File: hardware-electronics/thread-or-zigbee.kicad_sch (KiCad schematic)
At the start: 25 parts, among them U5 CP2102N-A02-GQFN20, U7 EFR32MG21B020F1024IM32-B

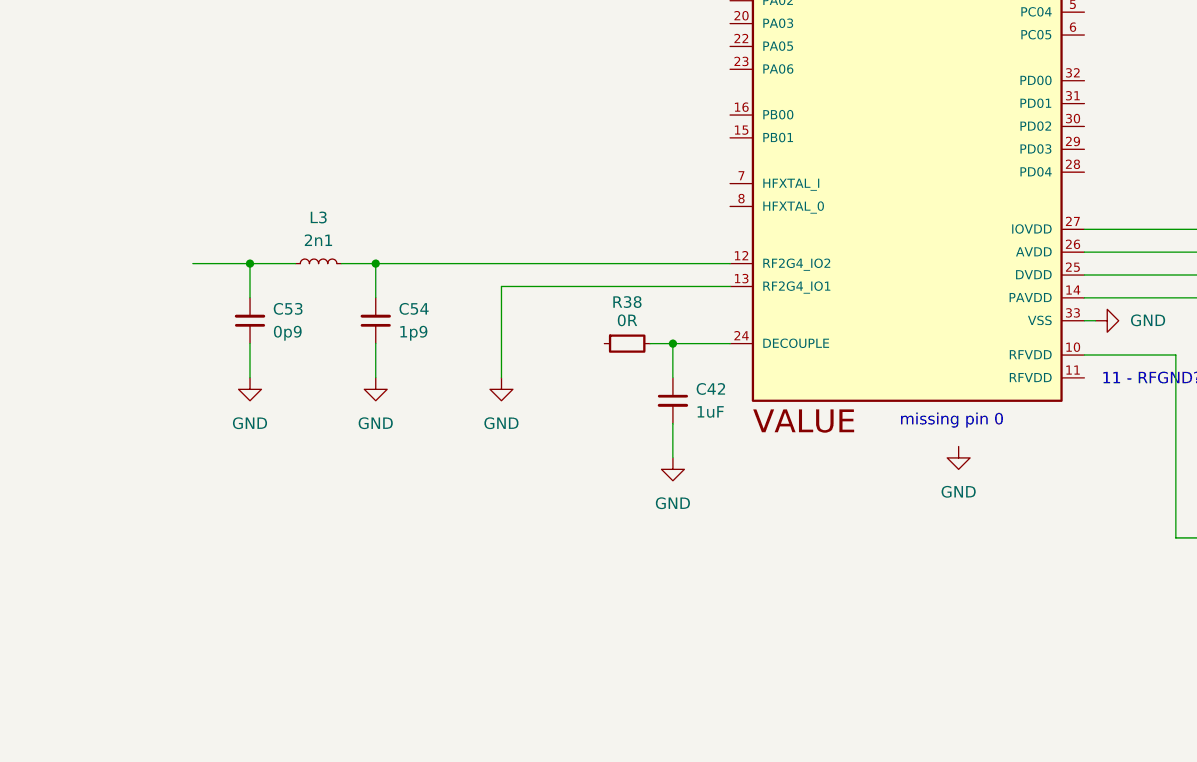
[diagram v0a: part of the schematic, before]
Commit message: #12 WIP SCH thread/zigbee working on EFR32MG21 add crystal oscillator
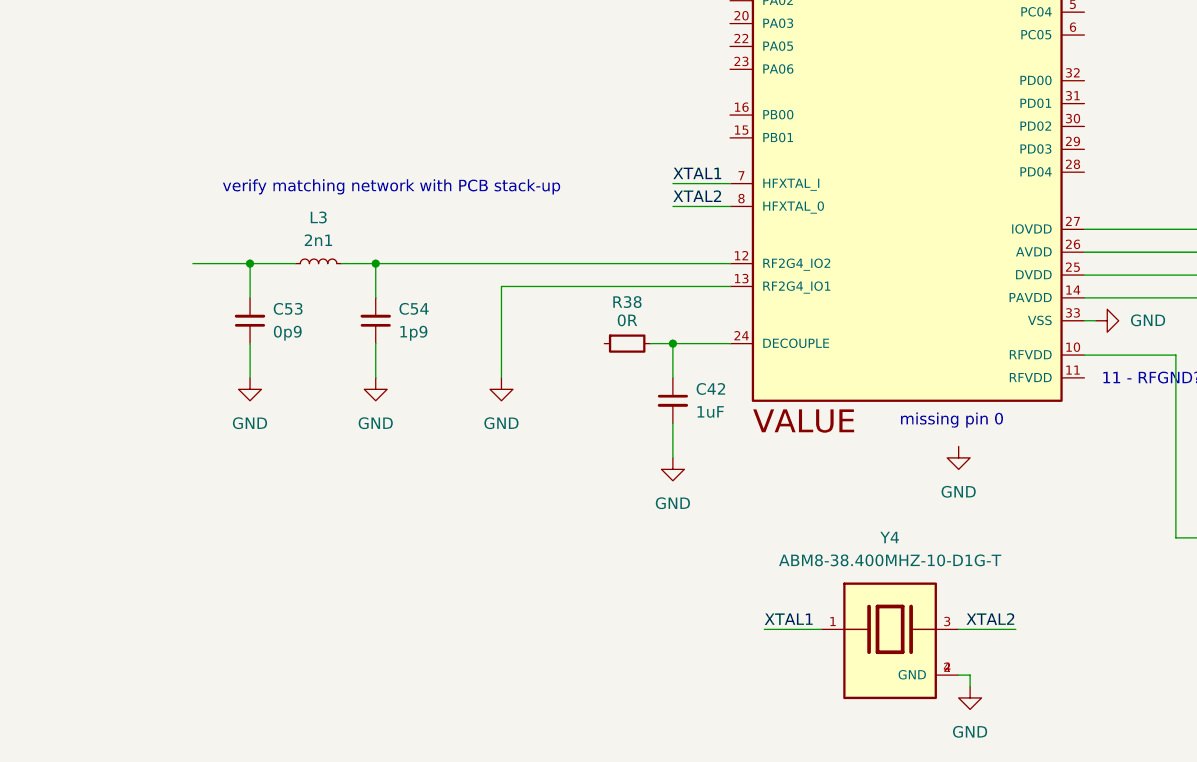
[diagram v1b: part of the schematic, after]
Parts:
- added Y4: ABM8-38.400MHZ-10-D1G-T, ABM8-38.400MHZ-10-D1G-T:XTAL_ABM8-38.400MHZ-10-D1G-T, symbol M2SmartHomeSymbols:ABM8-38.400MHZ-10-D1G-T
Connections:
- net GND: now also Y4.2 (GND), Y4.4 (GND)
- net XTAL1: now reaches U7.7 (HFXTAL_I)
- net XTAL1: now also Y4.1
- net XTAL2: now reaches U7.8 (HFXTAL_0)
- net XTAL2: now also Y4.3
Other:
- note added: "verify matching network with PCB stack-up"

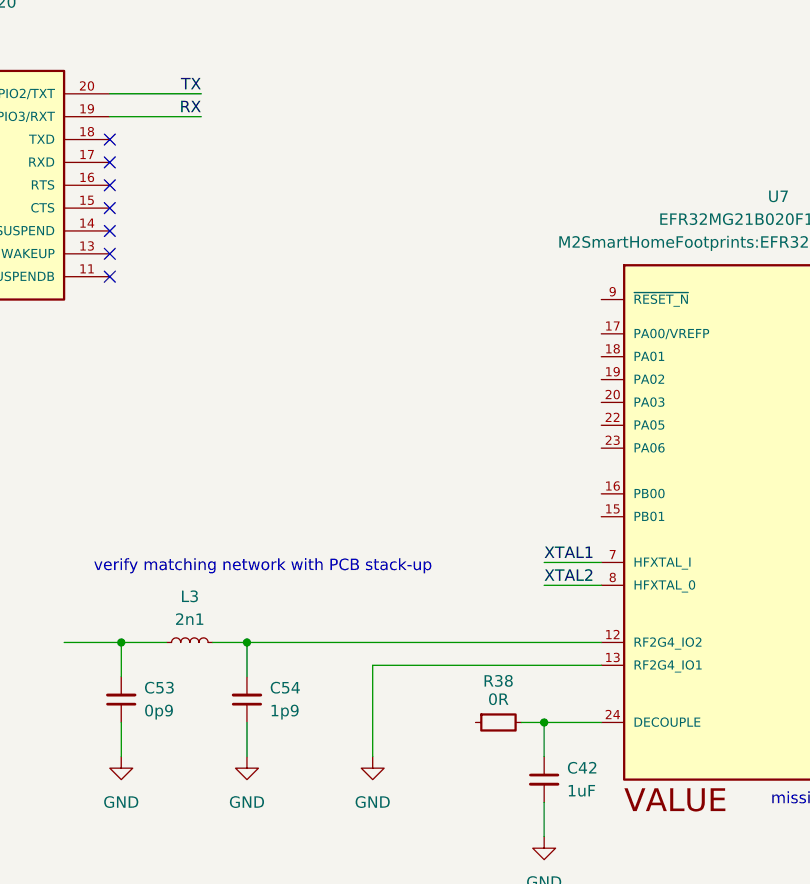
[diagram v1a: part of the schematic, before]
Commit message: #12 WIP SCH thread/zigbee working on EFR32MG21 connected decouple
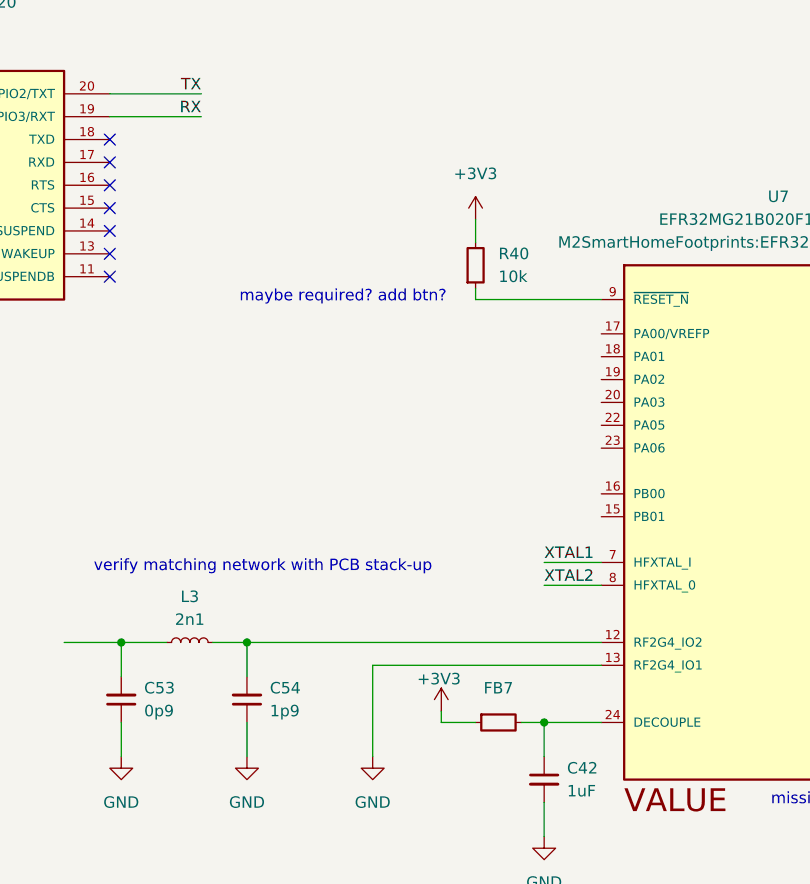
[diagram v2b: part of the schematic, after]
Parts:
- removed R38: R_0_0402, R_0_0402:R_0402_1005Metric, symbol M2SmartHomeSymbols:R_0_0402
- added FB7: FB_120R_0603, FB_120R_0603:FB_0603_1608Metric, symbol M2SmartHomeSymbols:FB_120R_0603
- added R40: R_10k_0402, R_10k_0402:R_0402_1005Metric, symbol M2SmartHomeSymbols:R_10k_0402
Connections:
- net +3V3: now also FB7.1, R40.2
- net at C42.1, U7.24 (DECOUPLE): now also FB7.2
- net at U7.9 (~{RESET_N}): now also R40.1
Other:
- note added: "maybe required? add btn?"

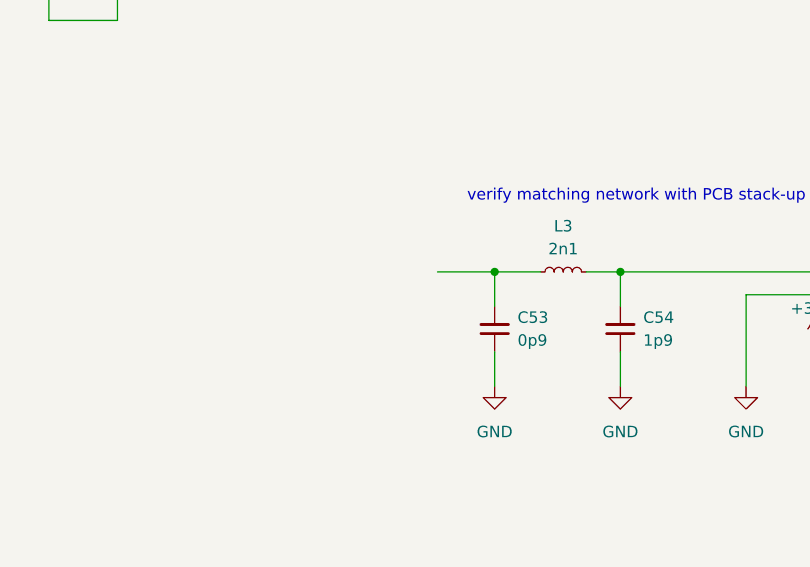
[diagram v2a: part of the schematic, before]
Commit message: #12 WIP SCH thread/zigbee working on EFR32MG21 add U.FL connector
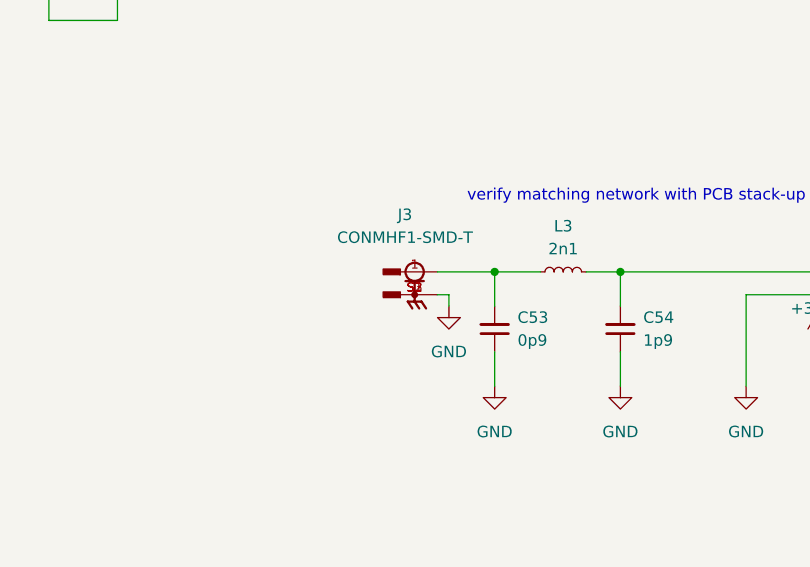
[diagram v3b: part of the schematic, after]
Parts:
- added J3: CONMHF1-SMD-T, CONMHF1-SMD-T:LINX_CONMHF1-SMD-T, symbol M2SmartHomeSymbols:CONMHF1-SMD-T
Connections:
- net GND: now also J3.S1, J3.S2, J3.S3
- net at C53.2, L3.1: now also J3.1

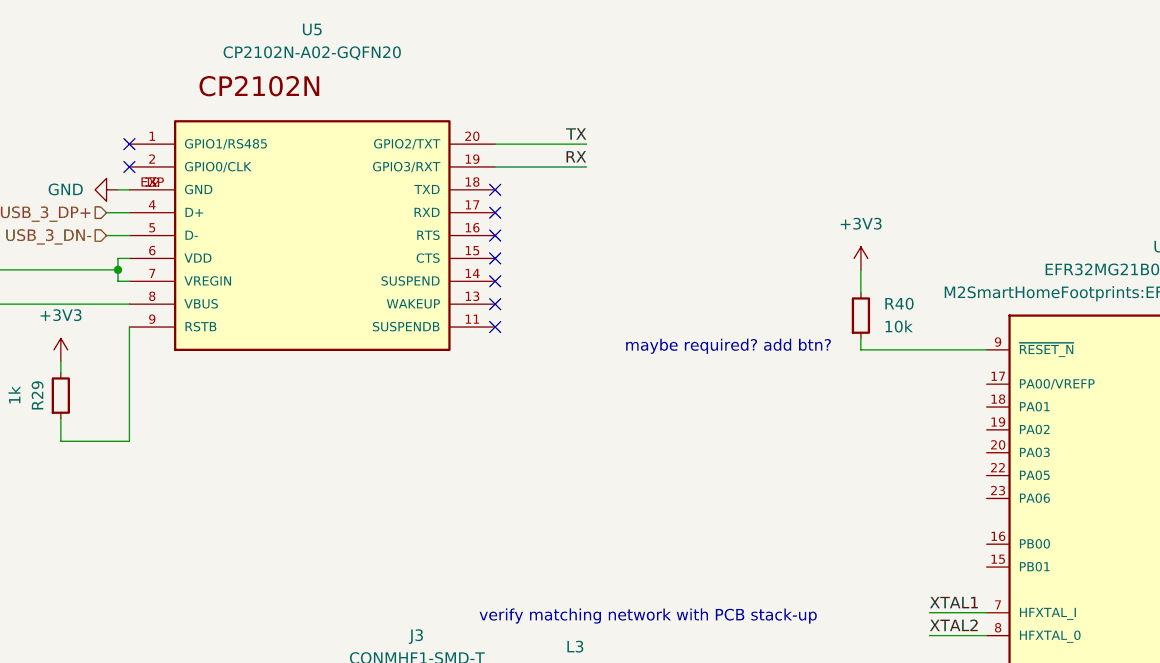
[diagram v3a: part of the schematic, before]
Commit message: [#12] SCH thread/zigbee correct UART
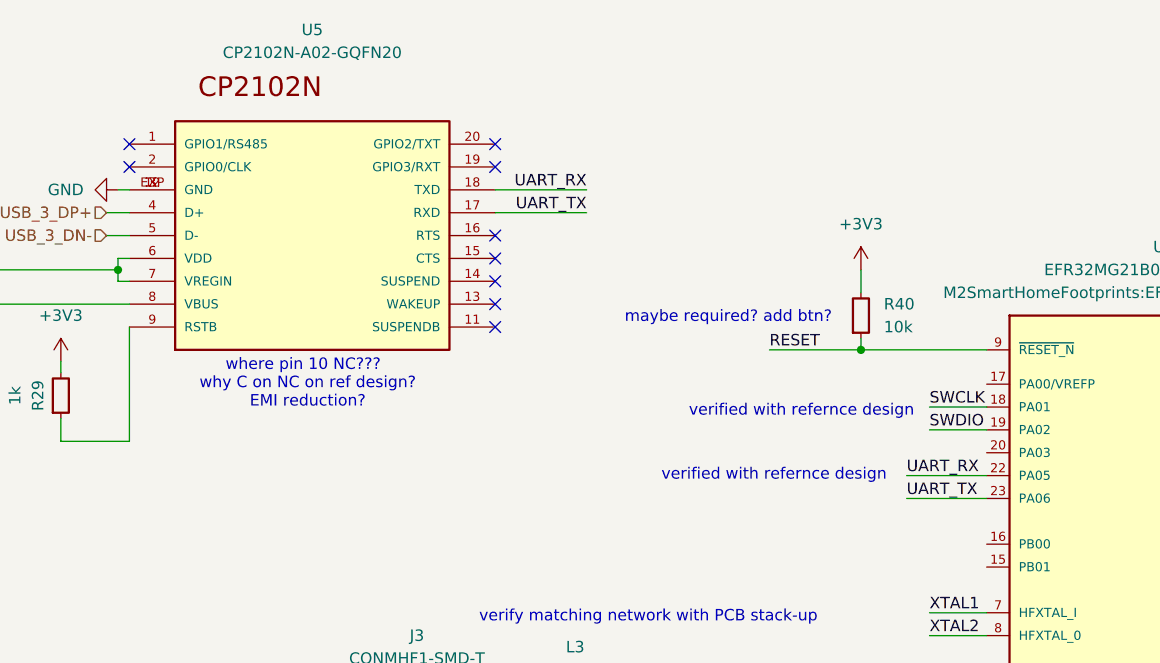
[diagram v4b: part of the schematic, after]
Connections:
- net SWCLK: now reaches U7.18 (PA01)
- net SWDIO: now reaches U7.19 (PA02)
- net UART_RX: now reaches U7.22 (PA05)
- net UART_RX: now also U5.18 (TXD)
- net UART_TX: now reaches U7.23 (PA06)
- net UART_TX: now also U5.17 (RXD)
- net RESET: now reaches R40.1, U7.9 (~{RESET_N})
- net RX: no longer names the net of U5.19 (GPIO3/RXT)
- net TX: no longer names the net of U5.20 (GPIO2/TXT)
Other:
- note added: "verified with refernce design"
- note added: "where pin 10 NC???"
- note added: "why C on NC on ref design? EMI reduction?"
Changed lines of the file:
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@@
+	)
+	(junction
+		(at 148.59 58.42)
+		(diameter 0)
+		(color 0 0 0 0)
 	)
 	(junction
@@
 	)
 	(no_connect
+		(at 107.95 38.1)
+	)
+	(no_connect
 		(at 107.95 50.8)
 	)
@@
 	)
 	(no_connect
-		(at 107.95 40.64)
-	)
-	(no_connect
-		(at 107.95 43.18)
+		(at 107.95 35.56)
 	)
 	(wire
@@
 	(wire
 		(pts
+			(xy 156.21 67.31) (xy 162.56 67.31)
+		)
+		(stroke
+			(width 0)
+			(type default)
+		)
+	)
+	(wire
+		(pts
 			(xy 166.37 137.16) (xy 172.72 137.16)
 		)
@@
 	(wire
 		(pts
+			(xy 156.21 64.77) (xy 162.56 64.77)
+		)
+		(stroke
+			(width 0)
+			(type default)
+		)
+	)
+	(wire
+		(pts
 			(xy 267.97 104.14) (xy 267.97 106.68)
 		)
@@
 	(wire
 		(pts
-			(xy 107.95 35.56) (xy 118.11 35.56)
-		)
-		(stroke
-			(width 0)
-			(type default)
-		)
-	)
-	(wire
-		(pts
 			(xy 153.67 105.41) (xy 156.21 105.41)
 		)
@@
 	(wire
 		(pts
+			(xy 153.67 74.93) (xy 162.56 74.93)
+		)
+		(stroke
+			(width 0)
+			(type default)
+		)
+	)
+	(wire
+		(pts
+			(xy 138.43 58.42) (xy 148.59 58.42)
+		)
+		(stroke
+			(width 0)
+			(type default)
+		)
+	)
+	(wire
+		(pts
 			(xy 27.94 60.96) (xy 31.75 60.96)
 		)
@@
 	(wire
 		(pts
-			(xy 107.95 38.1) (xy 118.11 38.1)
-		)
-		(stroke
-			(width 0)
-			(type default)
-		)
-	)
-	(wire
-		(pts
 			(xy 104.14 99.06) (xy 104.14 100.33)
 		)
@@
 	(wire
 		(pts
+			(xy 107.95 40.64) (xy 118.11 40.64)
+		)
+		(stroke
+			(width 0)
+			(type default)
+		)
+	)
+	(wire
+		(pts
+			(xy 153.67 72.39) (xy 162.56 72.39)
+		)
+		(stroke
+			(width 0)
+			(type default)
+		)
+	)
+	(wire
+		(pts
 			(xy 223.52 97.79) (xy 223.52 99.06)
 		)
@@
 		(pts
 			(xy 240.03 123.19) (xy 240.03 127)
+		)
+		(stroke
+			(width 0)
+			(type default)
+		)
+	)
+	(wire
+		(pts
+			(xy 107.95 43.18) (xy 118.11 43.18)
 		)
 		(stroke
@@
 		)
 	)
+	(text "verified with refernce design"
+		(exclude_from_sim no)
+		(at 141.986 65.278 0)
+		(effects
+			(font
+				(size 1.27 1.27)
+			)
+		)
+	)
 	(text "missing pin 0"
 		(exclude_from_sim no)
@@
 		)
 	)
+	(text "why C on NC on ref design?\nEMI reduction?"
+		(exclude_from_sim no)
+		(at 87.122 63.246 0)
+		(effects
+			(font
+				(size 1.27 1.27)
+			)
+		)
+	)
+	(text "where pin 10 NC???\n"
+		(exclude_from_sim no)
+		(at 86.614 60.198 0)
+		(effects
+			(font
+				(size 1.27 1.27)
+			)
+		)
+	)
 	(text "11 - RFGND???"
 		(exclude_from_sim no)
@@
 	(text "maybe required? add btn?"
 		(exclude_from_sim no)
-		(at 133.858 58.166 0)
+		(at 133.858 54.864 0)
+		(effects
+			(font
+				(size 1.27 1.27)
+			)
+		)
+	)
+	(text "verified with refernce design"
+		(exclude_from_sim no)
+		(at 138.938 72.39 0)
 		(effects
 			(font
@@
 		)
 	)
-	(label "TX"
-		(at 118.11 35.56 180)
+	(label "SWCLK"
+		(at 156.21 64.77 0)
+		(fields_autoplaced yes)
+		(effects
+			(font
+				(size 1.27 1.27)
+			)
+			(justify left bottom)
+		)
+	)
+	(label "UART_RX"
+		(at 153.67 72.39 0)
+		(fields_autoplaced yes)
+		(effects
+			(font
+				(size 1.27 1.27)
+			)
+			(justify left bottom)
+		)
+	)
+	(label "RESET"
+		(at 138.43 58.42 0)
+		(fields_autoplaced yes)
+		(effects
+			(font
+				(size 1.27 1.27)
+			)
+			(justify left bottom)
+		)
+	)
+	(label "UART_TX"
+		(at 118.11 43.18 180)
 		(fields_autoplaced yes)
 		(effects
@@
 		)
 	)
+	(label "UART_RX"
+		(at 118.11 40.64 180)
+		(fields_autoplaced yes)
+		(effects
+			(font
+				(size 1.27 1.27)
+			)
+			(justify right bottom)
+		)
+	)
+	(label "SWDIO"
+		(at 156.21 67.31 0)
+		(fields_autoplaced yes)
+		(effects
+			(font
+				(size 1.27 1.27)
+			)
+			(justify left bottom)
+		)
+	)
 	(label "XTAL2"
 		(at 156.21 90.17 0)
@@
 		)
 	)
-	(label "RX"
-		(at 118.11 38.1 180)
-		(fields_autoplaced yes)
-		(effects
-			(font
-				(size 1.27 1.27)
-			)
-			(justify right bottom)
-		)
-	)
 	(label "XTAL2"
 		(at 194.31 137.16 180)
@@
 		)
 	)
+	(label "UART_TX"
+		(at 153.67 74.93 0)
+		(fields_autoplaced yes)
+		(effects
+			(font
+				(size 1.27 1.27)
+			)
+			(justify left bottom)
+		)
+	)

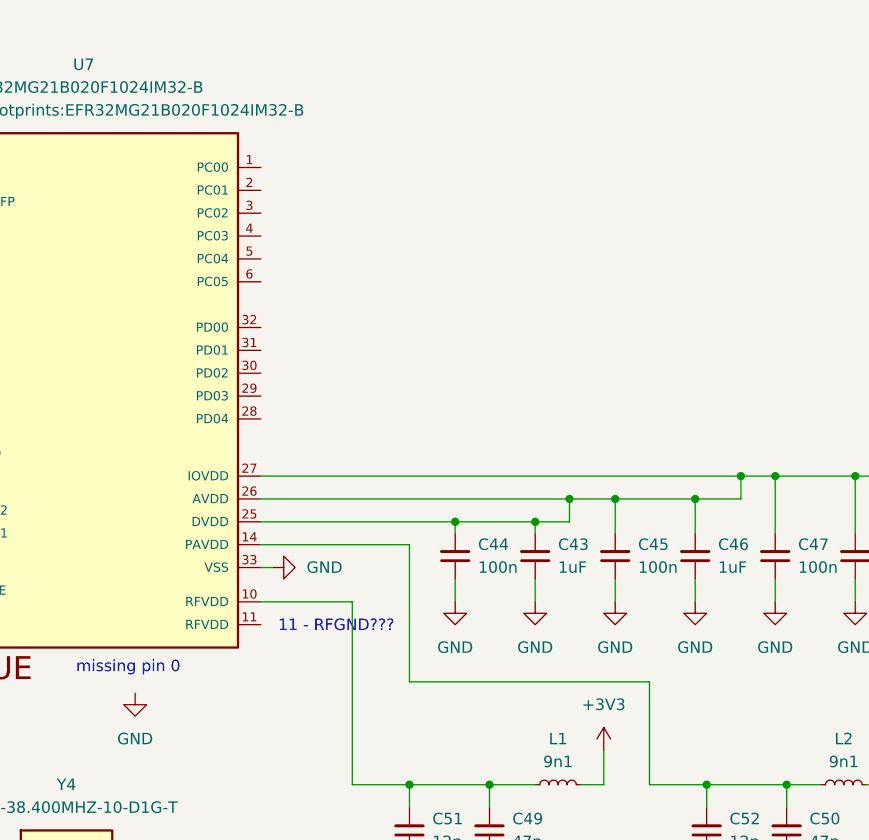
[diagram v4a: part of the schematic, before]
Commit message: [#12] SCH thread/zigbee EFR32 connections WIP
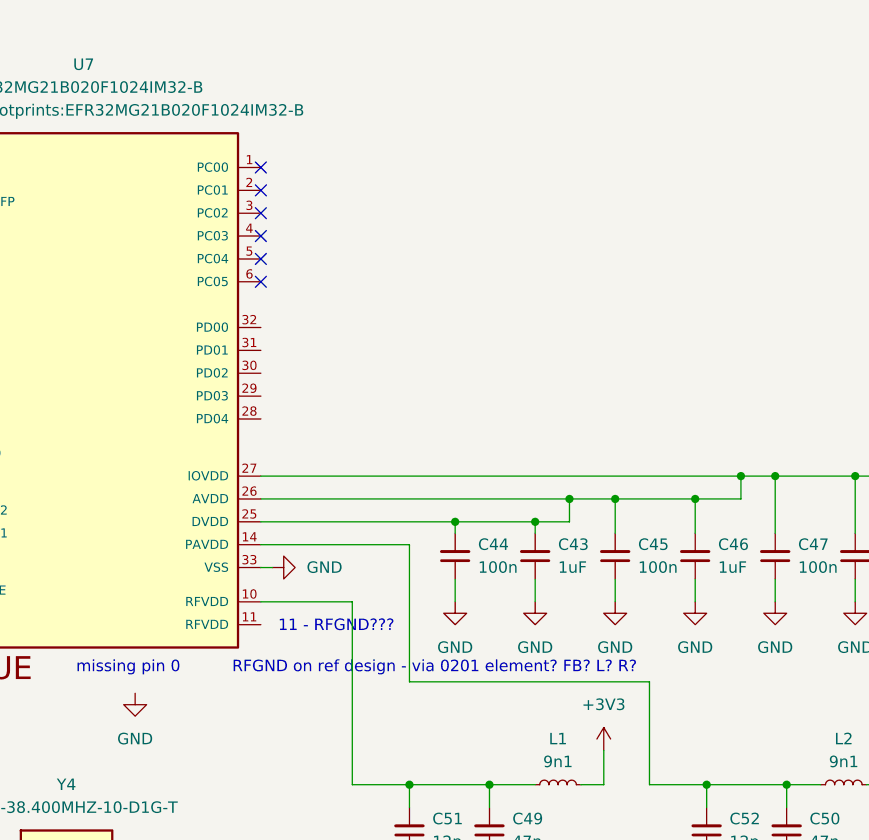
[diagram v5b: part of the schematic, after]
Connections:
- no-connect marks 9 -> 15
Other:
- note added: "RFGND on ref design - via 0201 element? FB? L? R?"
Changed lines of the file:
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@@
+	)
+	(no_connect
+		(at 201.93 68.58)
+	)
+	(no_connect
+		(at 201.93 66.04)
 	)
 	(no_connect
@@
 	)
 	(no_connect
+		(at 201.93 63.5)
+	)
+	(no_connect
+		(at 201.93 71.12)
+	)
+	(no_connect
 		(at 107.95 45.72)
 	)
 	(no_connect
+		(at 201.93 60.96)
+	)
+	(no_connect
 		(at 107.95 53.34)
 	)
@@
 	(no_connect
 		(at 107.95 35.56)
+	)
+	(no_connect
+		(at 201.93 58.42)
 	)
 	(wire
@@
 		(effects
 			(font
+				(size 1.27 1.27)
+			)
+		)
+	)
+	(text "RFGND on ref design - via 0201 element? FB? L? R?"
+		(exclude_from_sim no)
+		(at 221.234 114.046 0)
+		(effects
+			(font
